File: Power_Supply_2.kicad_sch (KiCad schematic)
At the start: 12 parts

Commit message: VER2.2: все изменения в списке изменений
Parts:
- removed D17, D4: WRA1215S-3WR2, Mornsun:WRA_S-3WR2, symbol Morsun:WRA1215S-3WR2
- added D17, D4: ~, DCDC_My:QA, symbol DCDC_My:QA1
- added L10, L9: 47u, Inductor_SMD:L_1812_4532Metric_Pad1.30x3.40mm_HandSolder, symbol Device:L
- C12, C13, C16, C39: value 10u -> 4.7u; footprint Capacitor_SMD:C_1210_3225Metric_Pad1.33x2.70mm_HandSolder -> Capacitor_SMD:C_1206_3216Metric_Pad1.33x1.80mm_HandSolder
- L3, L5: value 4.7u -> 12u; footprint Inductor_SMD:L_1812_4532Metric_Pad1.30x3.40mm_HandSolder -> Inductor_SMD:L_1210_3225Metric_Pad1.42x2.65mm_HandSolder; Product Name (none) -> LQH32MN120J23L
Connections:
- net +15V_H2: now also D4.7 (+Vo)
- net +15V_L2: now also D17.7 (+Vo)
- net -15V_H2: now also D4.5 (-Vo)
- net -15V_L2: now also D17.5 (-Vo)
- net E3: now also D4.6 (0V)
- net E4: now also D17.6 (0V)
- net GND: now also D17.2 (GND), D4.2 (GND)
- net at C39.1, L5.2: now also L10.1
- net at C13.1, L3.2: now also L9.1
- new net: D17.1 (Vin), L10.2
- new net: D4.1 (Vin), L9.2
- no-connect marks 2 -> 0
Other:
- moved on the sheet: C11, C12, C13, C14, C15, C16, C39, C43, L3, L5

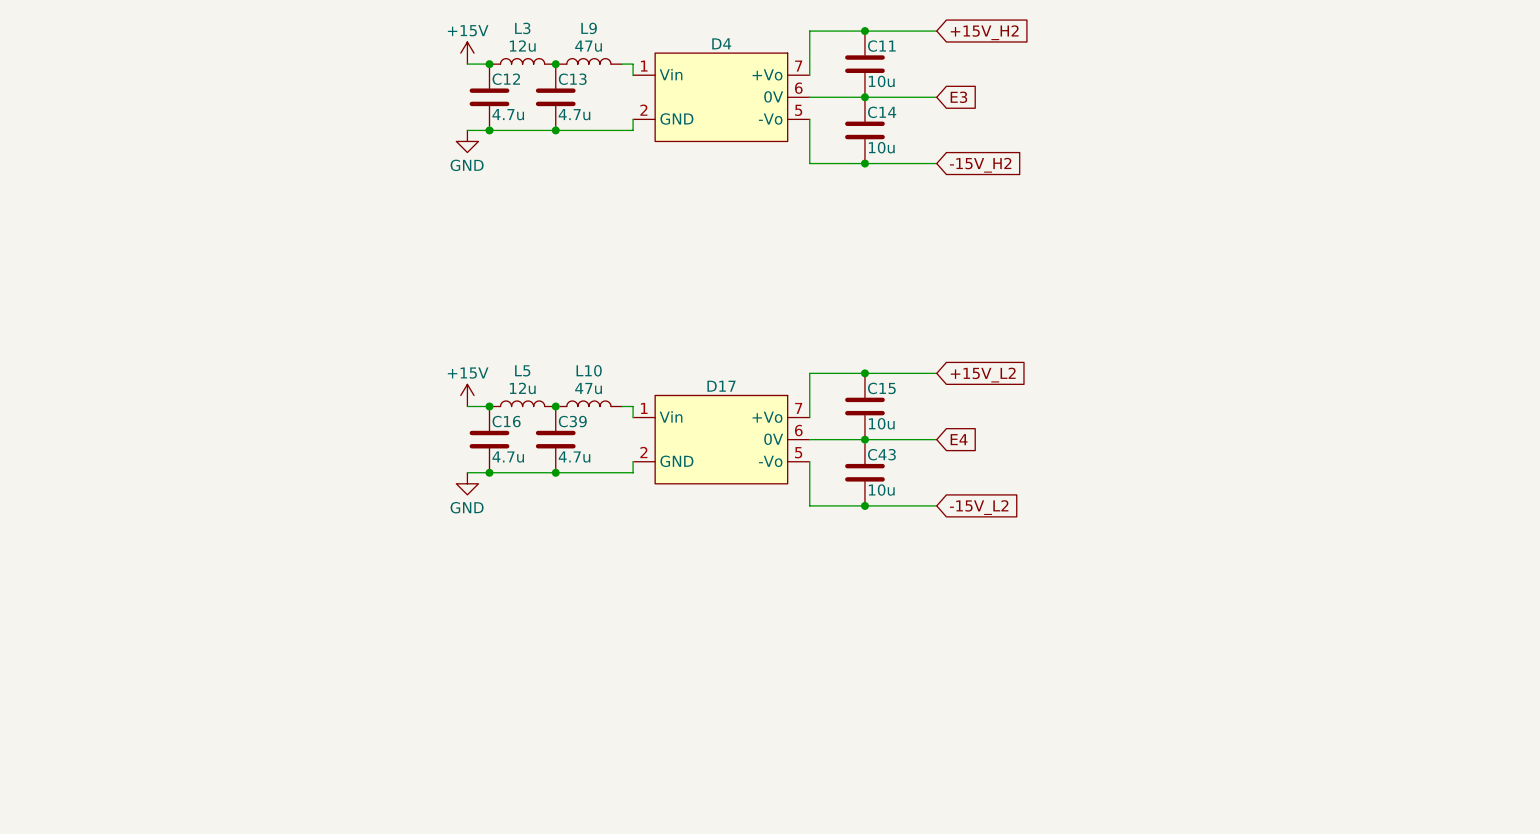
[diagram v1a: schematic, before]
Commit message: VER2.2: добавил фильтры на вход ШИМа и обновил все доки
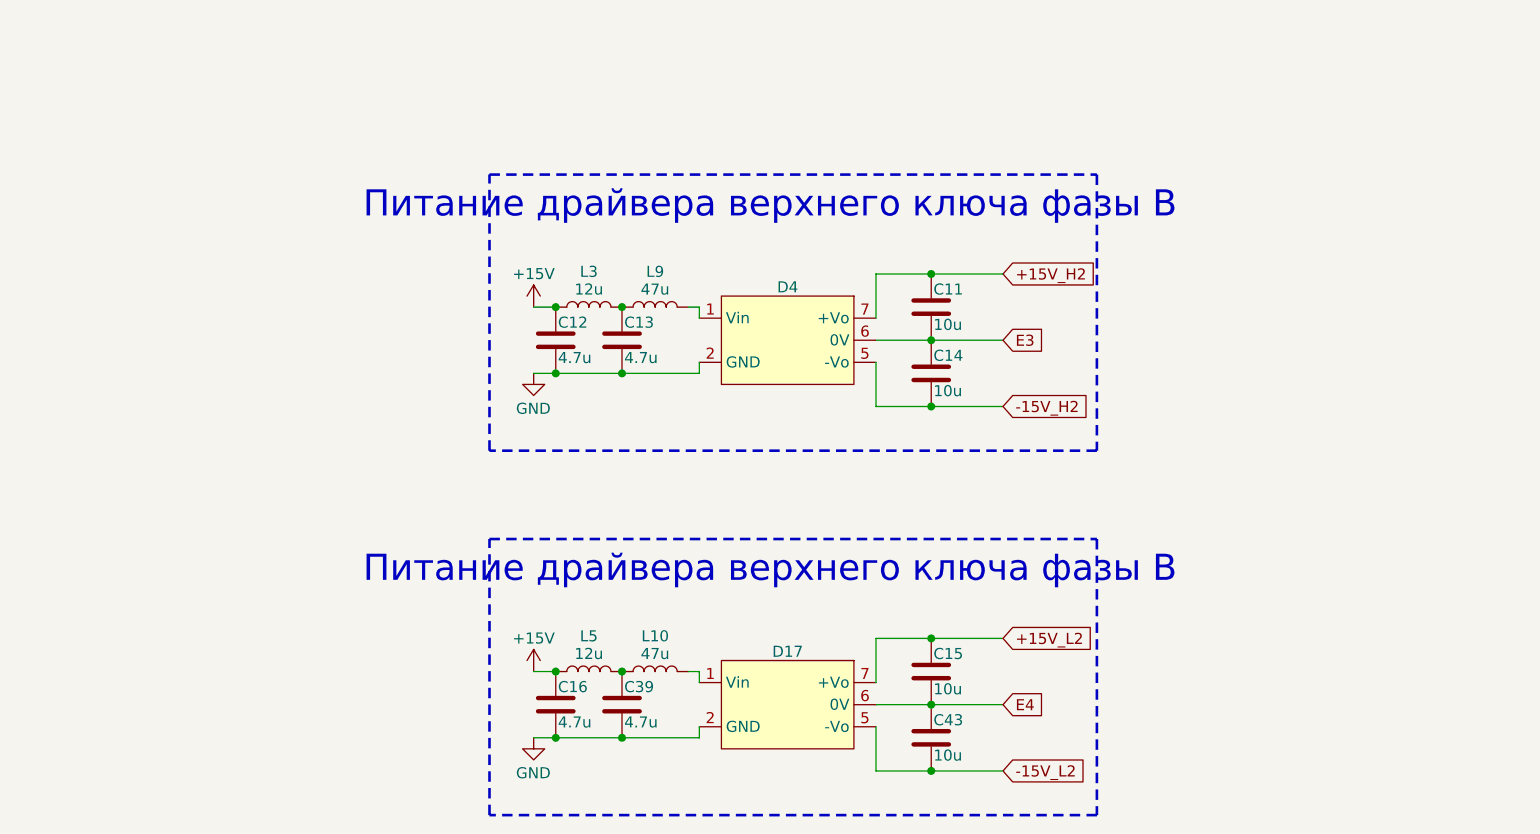
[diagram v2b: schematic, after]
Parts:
- L10, L3, L5, L9: Description P/N (none) -> Inductor SMD
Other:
- note added: "Питание драйвера верхнего ключа фазы В"
- company: (none) -> ООО "ЭТТ"
- moved on the sheet: C11, C12, C13, C14, C15, C16, C39, C43, D17, D4, L10, L3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

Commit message: VER2.2.1: создал папку для производственных доков
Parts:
- C11, C14, C15, C43: Description P/N (none) -> Capacitor SMD 50+V
- C12, C13, C16, C39: Description P/N (none) -> Capacitor SMD 25+V
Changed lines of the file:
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@@
 			)
 		)
-		(property "Description P/N" ""
+		(property "Description P/N" "Capacitor SMD 50+V"
 			(at 171.45 130.81 0)
 			(effects
@@
 			)
 		)
-		(property "Description P/N" ""
+		(property "Description P/N" "Capacitor SMD 25+V"
 			(at 135.89 127 0)
 			(effects
@@
 			)
 		)
-		(property "Description P/N" ""
+		(property "Description P/N" "Capacitor SMD 50+V"
 			(at 171.45 81.28 0)
 			(effects
@@
 			)
 		)
-		(property "Description P/N" ""
+		(property "Description P/N" "Capacitor SMD 50+V"
 			(at 171.45 88.9 0)
 			(effects
@@
 			)
 		)
-		(property "Description P/N" ""
+		(property "Description P/N" "Capacitor SMD 25+V"
 			(at 128.27 85.09 0)
 			(effects
@@
 			)
 		)
-		(property "Description P/N" ""
+		(property "Description P/N" "Capacitor SMD 25+V"
 			(at 135.89 85.09 0)
 			(effects
@@
 			)
 		)
-		(property "Description P/N" ""
+		(property "Description P/N" "Capacitor SMD 50+V"
 			(at 171.45 123.19 0)
 			(effects
@@
 			)
 		)
-		(property "Description P/N" ""
+		(property "Description P/N" "Capacitor SMD 25+V"
 			(at 128.27 127 0)
 			(effects
